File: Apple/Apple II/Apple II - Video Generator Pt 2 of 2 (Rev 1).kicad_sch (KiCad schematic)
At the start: 0 parts

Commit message: Finished Apple II - Sheet 18 - Video Generator Part 2 (Rev 1)
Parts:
- added A12: 74LS02, symbol Apple II:A12_74LS02
- added B14: 74LS02, symbol Apple II:B14_74LS02
- added B?: 74LS08, symbol Apple II:B11_74LS08
- added B?: 74LS02, symbol Apple II:B13_74LS02
- added B?: 74LS11, symbol Apple II:B12_74LS11
- added C11: 74LS04, symbol Apple II:C11_74LS04
- added C2: 47pF, symbol Device:C_Small
- added C3: 5-50pF, symbol Device:C_Variable
- added C?: 74LS32, symbol Apple II:C14_74LS32
- added J?: AUX VIDEO CONNECTOR, symbol Connector:Conn_01x04_Male
- added J?: COMPOSITE VIDEO OUTPUT, symbol Connector:Conn_Coaxial
- added J?: AUX VIDEO PIN, symbol Connector:Conn_01x01_Male
- added JP12: 12, symbol Apple II:Bowtie_SolderJumper
- added JP13: 13, symbol Jumper:SolderJumper_2_Open
- added JP14: 14, symbol Jumper:SolderJumper_2_Open
- added JP16: 16, symbol Apple II:Bowtie_SolderJumper
- added L1: 27µH, symbol Device:L
- added Q3, Q6: 2N3904, Package_TO_SOT_THT:TO-92_Inline, symbol Transistor_BJT:2N3904
- added R10: 27Ω, symbol Device:R_US
- added R11: 200Ω, symbol Device:R_Potentiometer_US
- added R27: 4.7K, symbol Device:R_US
- added R5: 1K, symbol Device:R_US
- added R6: 2.7K, symbol Device:R_US
- added R7: 1.5K, symbol Device:R_US
- added R8: 2K, symbol Device:R_US
- added R9: 10Ω, symbol Device:R_US
- added U? (x2): C13_74LS51, symbol Apple II:C13_74LS51
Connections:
- new net: B14.1, U?.1
- new net: B14.2, JP12.2 (B), JP13.2 (B)
- new net: B14.3, B14.4
- new net: Q3.2 (B), R6.2, R7.2, R8.2
- new net: J?.2 (Pin_2), Q3.1 (E), R11.1
- new net: B14.11, JP14.2 (B), JP16.2 (B)
- new net: C2.1, C3.1, L1.1, Q6.3 (C), R5.2, R6.1
- new net: B14.13, U?.12
- new net: B?.8, C?.4, U?.13
- new net: C11.10, JP12.1 (A)
- new net: J?.1 (In), R10.2
- new net: B?.1, B?.1
- new net: J?.1 (Pin_1), R10.1, R11.2
- new net: A12.4, B14.12
- new net: A12.5, A12.6, B14.10
- new net: Q6.2 (B), R27.2
- new net: Q3.3 (C), R9.1
- new net +12V: J?.4 (Pin_4)
- new net +5V: R9.2
- new net -5V: J?.3 (Pin_3)
- new net BLANKING: C?.6
- new net COLOR_BURST: B?.12, R5.1
- new net COLOR_REF_{35}: B?.2
- new net Earth: C2.2, C3.2, J?.1 (Pin_1), J?.2 (Ext), L1.2, Q6.1 (E), R11.3
- new net H2: B?.3
- new net H3: U?.10, U?.11, U?.3
- new net H4: B14.5, B?.2, U?.2
- new net H5: B14.6, U?.4, U?.5
- new net HBL: B?.13, C?.5, U?.6, U?.9
- new net SYNC_{19}: R8.1, U?.8
- new net TEXT MODE: R27.1
- new net V0: B14.9
- new net V1: JP16.1 (A)
- new net V2: C11.11, JP14.1 (A)
- new net V3: B?.9
- new net V4: B?.10
- new net V5: JP13.1 (A)
- new net VC: B14.8
- new net VIDEO_DATA: R7.1
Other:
- note added: "FROM CLOCK GENERATOR"
- note added: "FROM ON-BOARD I/O"
- note added: "FROM PART 1"
- note added: "FROM VIDEO ADDRESS GENERATOR"
- note added: "TO MEMORY ADDRESS PT 1"
- note added: "TO PART 1"
- note added: "TO PERIPHREAL I/O"
- title: (none) -> Apple II - Video Generator Part 2

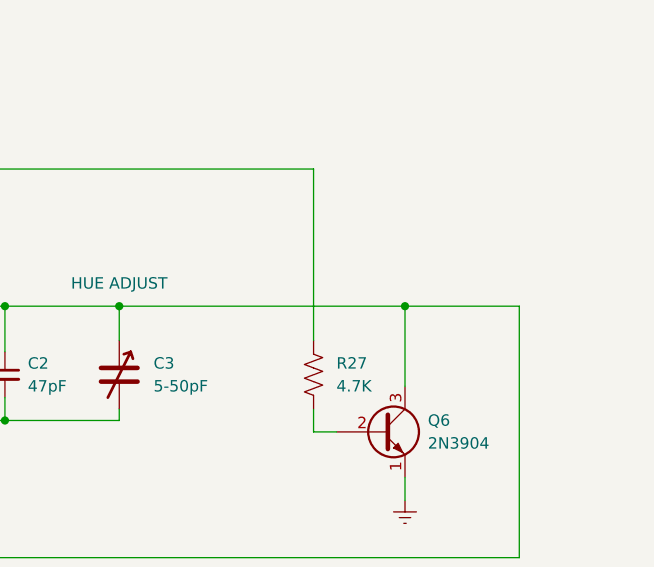
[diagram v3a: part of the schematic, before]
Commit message: Finished Apple II - Sheet 19 - Video Generator Part 2 (Rev 7)
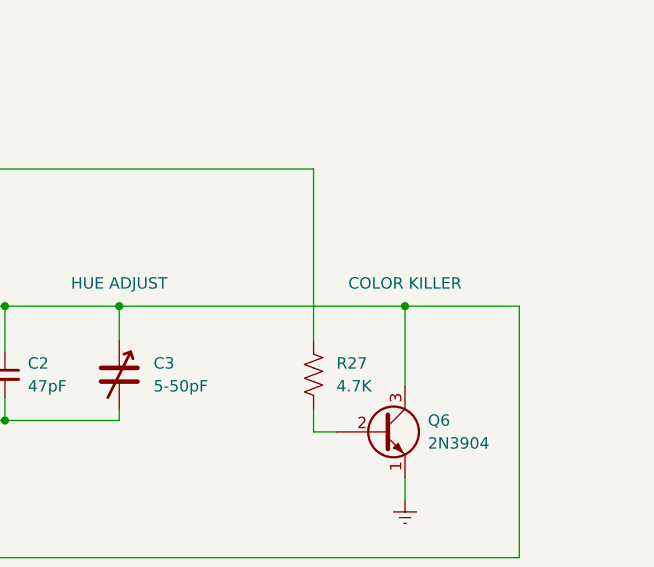
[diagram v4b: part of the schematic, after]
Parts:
- Q6: NAME (none) -> COLOR KILLER
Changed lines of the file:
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@@
   )
   (symbol (lib_id "Transistor_BJT:2N3904") (at 363.22 73.66 0) (unit 1)
-    (in_bom yes) (on_board yes) (fields_autoplaced)
+    (in_bom yes) (on_board yes)
     (property "Reference" "Q6" (id 0) (at 368.3 72.3899 0)
       (effects (font (size 1.27 1.27)) (justify left))
@@
       (effects (font (size 1.27 1.27)) (justify left) hide)
     )
+    (property "NAME" "COLOR KILLER" (id 4) (at 365.76 57.15 0))
     (pin "1")
     (pin "2")

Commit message: Finished Apple II - Sheet 22 - Two-Piece Keyboard
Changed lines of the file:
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@@
   (junction (at 77.47 170.18) (diameter 0) (color 0 0 0 0)
   )
-  (polyline (pts (xy 0 0) (xy 0 12.7))
-    (stroke (width 0) (type default) (color 0 0 0 0))
-  )
   (polyline (pts (xy 334.01 190.5) (xy 335.28 190.5))
     (stroke (width 0) (type solid) (color 0 0 0 0))
@@
     (stroke (width 0) (type default) (color 0 0 0 0))
   )
-  (polyline (pts (xy 12.7 0) (xy 0 0))
-    (stroke (width 0) (type default) (color 0 0 0 0))
-  )
